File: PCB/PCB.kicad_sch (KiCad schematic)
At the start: 41 parts, among them J1 USB_C_Receptacle_USB2.0_14P, J2 OLED_128x64, SW1 SW_Push, SW2 RotaryEncoder, SW3 RotaryEncoder, U1 STM32F072CBTx, U2 USBLC6-2SC6, U3 XC6206, U5 TRRS

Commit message: Updated
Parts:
- added J3: Micro_SD_Card_Det1, symbol Connector:Micro_SD_Card_Det1
- added R13, R14, R16, R17: 10k, symbol Device:R
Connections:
- net +3.3V: now also J3.4 (VDD), R13.1, R14.1, R16.1, R17.1
- net GND: now also J3.6 (VSS), J3.SH (SHIELD)
- net SLIDER_1: now also U1.13 (PA3); no longer U1.27 (PB14)
- net SLIDER_2: now also U1.12 (PA2); no longer U1.28 (PB15)
- net CS: now reaches U1.14 (PA4)
- net CS: now also J3.2 (DAT3/CD), R14.2
- net IS_SD: now reaches U1.15 (PA5)
- net IS_SD: now also J3.9 (DET), R17.2
- net SCK: now reaches U1.26 (PB13)
- net SCK: now also J3.5 (CLK)
- new net MISO: J3.7 (DAT0), R16.2, U1.27 (PB14)
- new net MOSI: J3.3 (CMD), R13.2, U1.28 (PB15)
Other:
- moved on the sheet: C7, H1, H2, H3, H4, H5, U1

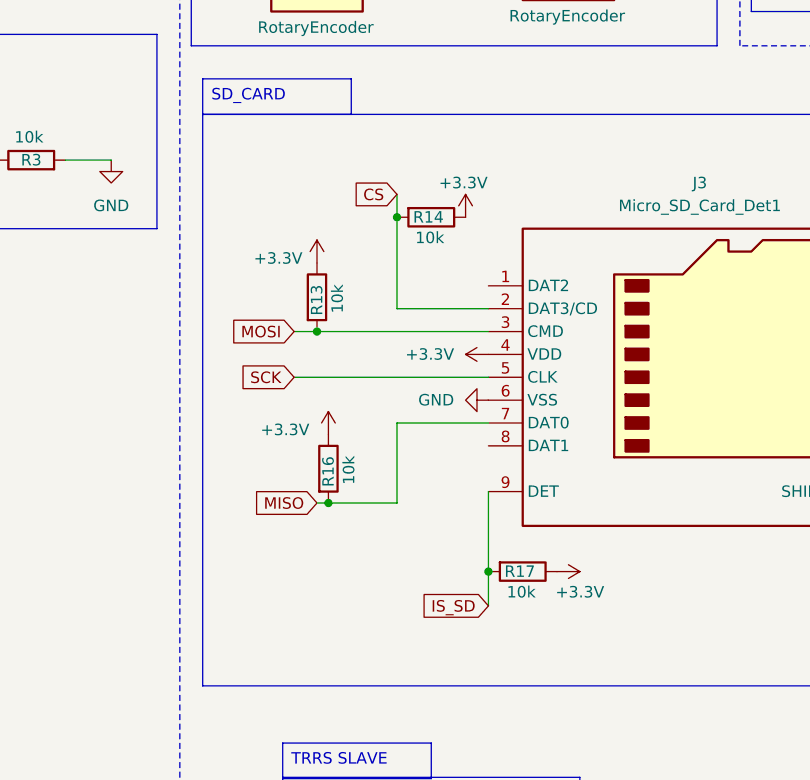
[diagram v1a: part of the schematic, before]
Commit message: Added sd card and fixed some wirings
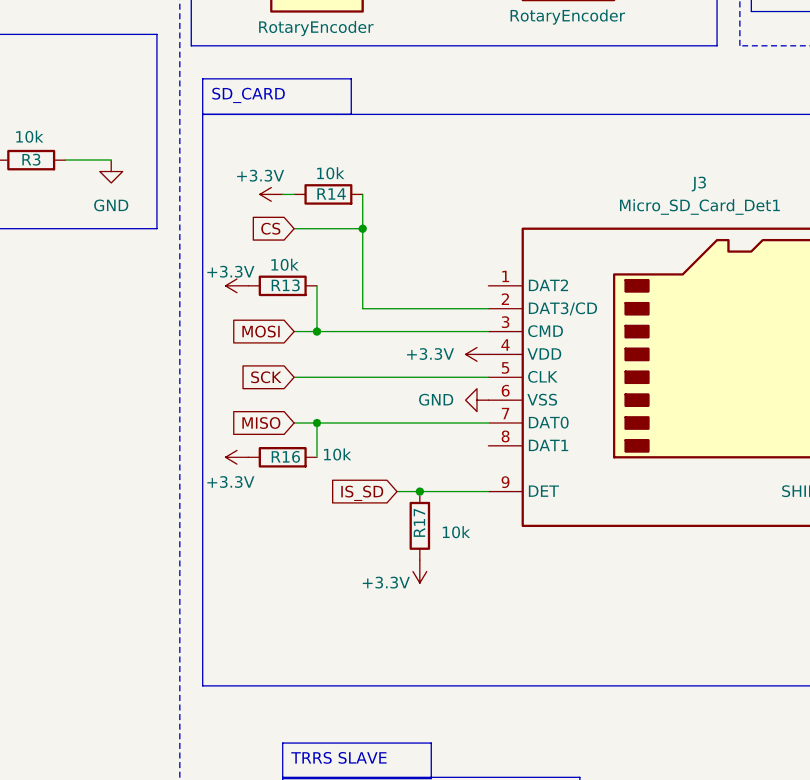
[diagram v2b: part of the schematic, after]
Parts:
- J3: footprint (none) -> Connector_Card:microSD_HC_Hirose_DM3AT-SF-PEJM5
- R13, R14, R16, R17: footprint (none) -> Resistor_SMD:R_0805_2012Metric
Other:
- moved on the sheet: R13, R14, R16, R17
